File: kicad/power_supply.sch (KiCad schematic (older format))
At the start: 12 parts, among them U1 TPS560430X

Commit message: Fix issues found during testing (v0.1.1)
- Add BAT+/- and EXT+/- markings to terminals (#2)
- Change C30 to 470nF (#5)
- Add C20 (47nF) at VC0 pin (#5)
- Add C21 and R72 for proper low-pass filter of VDD (#5)
- Change C39 at VREF to 1uF (#5)
- Add R70: Pull-down for PCHG FET (#5)
- Add R73: Weak pull-down for 5V supply (#6)
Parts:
- R28: value 54.9k -> 50.5k; PartNumber RC0603FR-0754K9L -> RC0603FR-0750K5L
- U1: symbol LibreSolar:LMR16006 -> bms-8s50-ic-rescue:LMR16006-LibreSolar
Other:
- note added: "Vref = 1V"
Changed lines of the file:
@@
 EESchema Schematic File Version 4
-LIBS:bms-8s50-ic-cache
-EELAYER 29 0
+EELAYER 30 0
 EELAYER END
 $Descr A4 11693 8268
@@
 Sheet 2 5
 Title "BMS 8S50 IC"
-Date "2017-05-27"
-Rev "0.1"
+Date "2020-05-08"
+Rev "0.1.1"
 Comp "Libre Solar"
 Comment1 "License: CC-BY-SA"
@@
 AR Path="/58363B12/5C685CF3" Ref="R28"  Part="1"
 F 0 "R28" V 6825 3400 50  0000 C CNN
-F 1 "54.9k" V 6975 3400 50  0000 C CNN
+F 1 "50.5k" V 6975 3400 50  0000 C CNN
 F 2 "LibreSolar:R_0603_1608" V 6725 3300 50  0001 C CNN
 F 3 "" H 6900 3400 50  0000 C CNN
 F 4 "Yageo" H 1200 800 50  0001 C CNN "Manufacturer"
-F 5 "RC0603FR-0754K9L" H 1200 800 50  0001 C CNN "PartNumber"
+F 5 "RC0603FR-0750K5L" H 1200 800 50  0001 C CNN "PartNumber"
 	1    6900 3400
 	1    0    0    -1
@@
 $EndComp
 $Comp
-L LibreSolar:LMR16006 U?
+L bms-8s50-ic-rescue:LMR16006-LibreSolar U?
 U 1 1 5C685D37
 P 5400 3200
 AR Path="/5C683890/5C685D37" Ref="U?"  Part="1"
 AR Path="/58363B12/5C685D37" Ref="U1"  Part="1"
+AR Path="/5C685D37" Ref="U1"  Part="1"
 F 0 "U1" H 5400 3550 50  0000 C CNN
 F 1 "TPS560430X" H 5400 2850 50  0000 C CNN
@@
 Text Notes 7200 2300 0    50   ~ 0
 ToDo: Check Bourns inductor part number\n(L2) and possibly reduce footprint size
+Text Notes 6200 3700 0    50   ~ 0
+Vref = 1V
 $EndSCHEMATC

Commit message: Add KiCad symbol cache and remove rescue lib
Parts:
- U1: symbol bms-8s50-ic-rescue:LMR16006-LibreSolar -> LibreSolar:LMR16006
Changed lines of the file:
@@
 $EndComp
 $Comp
-L bms-8s50-ic-rescue:LMR16006-LibreSolar U?
+L LibreSolar:LMR16006 U?
 U 1 1 5C685D37
 P 5400 3200

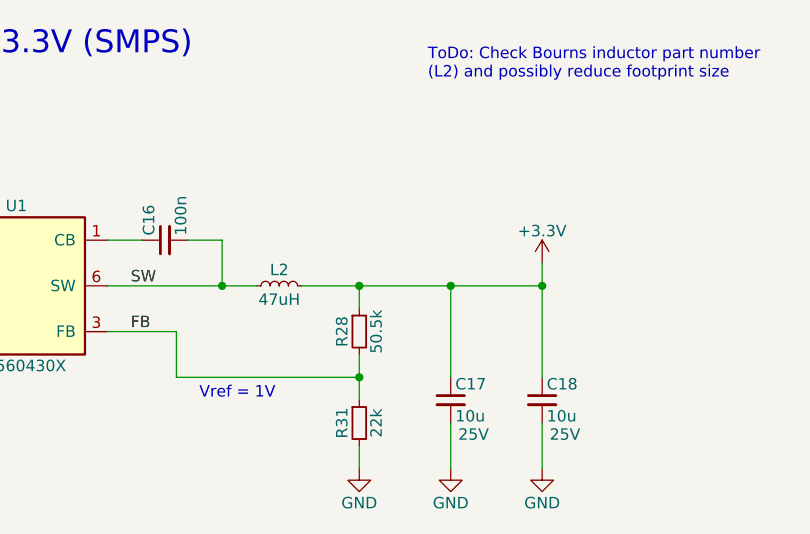
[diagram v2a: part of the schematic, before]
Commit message: Update to v0.2
- Switch to STM32L452 MCU (STM32F072 has too little RAM for CAN ISO-TP etc.)
- Add CAN termination jumper
- Add CAN bus power supply diodes
- Update CAN connector to match LS.bus spec
- Add interactive BOM and CSV BOM to build directory
- Add additional thermal vias with 0.2mm diameter under MOSFETs
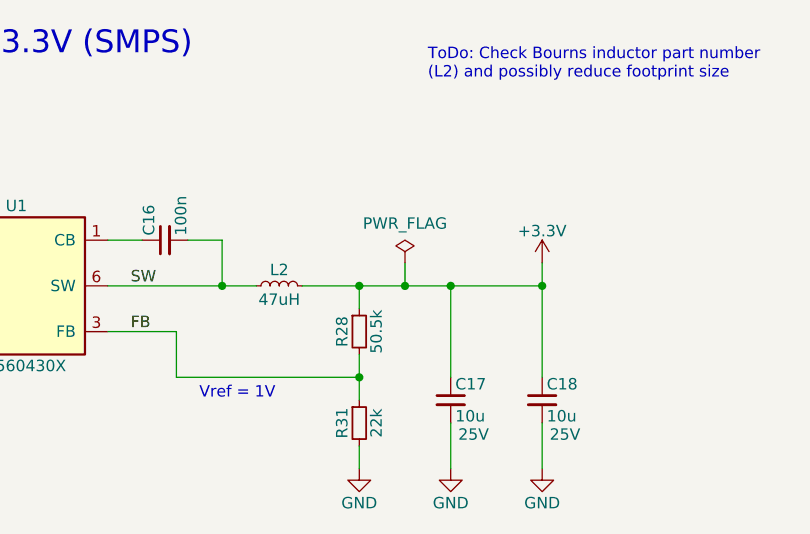
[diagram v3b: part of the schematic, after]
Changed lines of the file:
@@
 Sheet 2 5
 Title "BMS 8S50 IC"
-Date "2020-05-08"
-Rev "0.1.1"
-Comp "Libre Solar"
-Comment1 "License: CC-BY-SA"
+Date "2021-02-13"
+Rev "0.2"
+Comp "Libre Solar Technologies GmbH"
+Comment1 "Website: https://libre.solar"
 Comment2 "Author: Martin Jäger"
-Comment3 ""
+Comment3 "License: Creative Commons Attribution-ShareAlike 4.0 International"
 Comment4 ""
 $EndDescr
@@
 Connection ~ 4700 3000
 Wire Wire Line
-	6900 3200 7300 3200
+	6900 3200 7100 3200
 Wire Wire Line
 	3600 3000 3800 3000
@@
 $EndComp
 Wire Wire Line
-	2500 2600 2300 2600
-Wire Wire Line
 	3200 2500 3200 2600
 Wire Wire Line
@@
 Text Notes 6200 3700 0    50   ~ 0
 Vref = 1V
+Wire Wire Line
+	2500 2600 2300 2600
+$Comp
+L power:PWR_FLAG #FLG0103
+U 1 1 60546ECF
+P 7100 3100
+F 0 "#FLG0103" H 7100 3175 50  0001 C CNN
+F 1 "PWR_FLAG" H 7100 3273 50  0000 C CNN
+F 2 "" H 7100 3100 50  0001 C CNN
+F 3 "~" H 7100 3100 50  0001 C CNN
+	1    7100 3100
+	1    0    0    -1
+$EndComp
+Wire Wire Line
+	7100 3100 7100 3200
+Connection ~ 7100 3200
+Wire Wire Line
+	7100 3200 7300 3200
 $EndSCHEMATC
